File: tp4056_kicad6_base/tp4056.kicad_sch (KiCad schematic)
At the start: 23 parts, among them J1 USB_B_Micro, J2 Conn_01x01_Female, J3 Conn_01x01_Female, J4 Conn_01x01_Female, J5 Conn_01x01_Female, J6 Conn_01x01_Female, J7 Conn_01x01_Female, U1 TP4056, U2 DW01

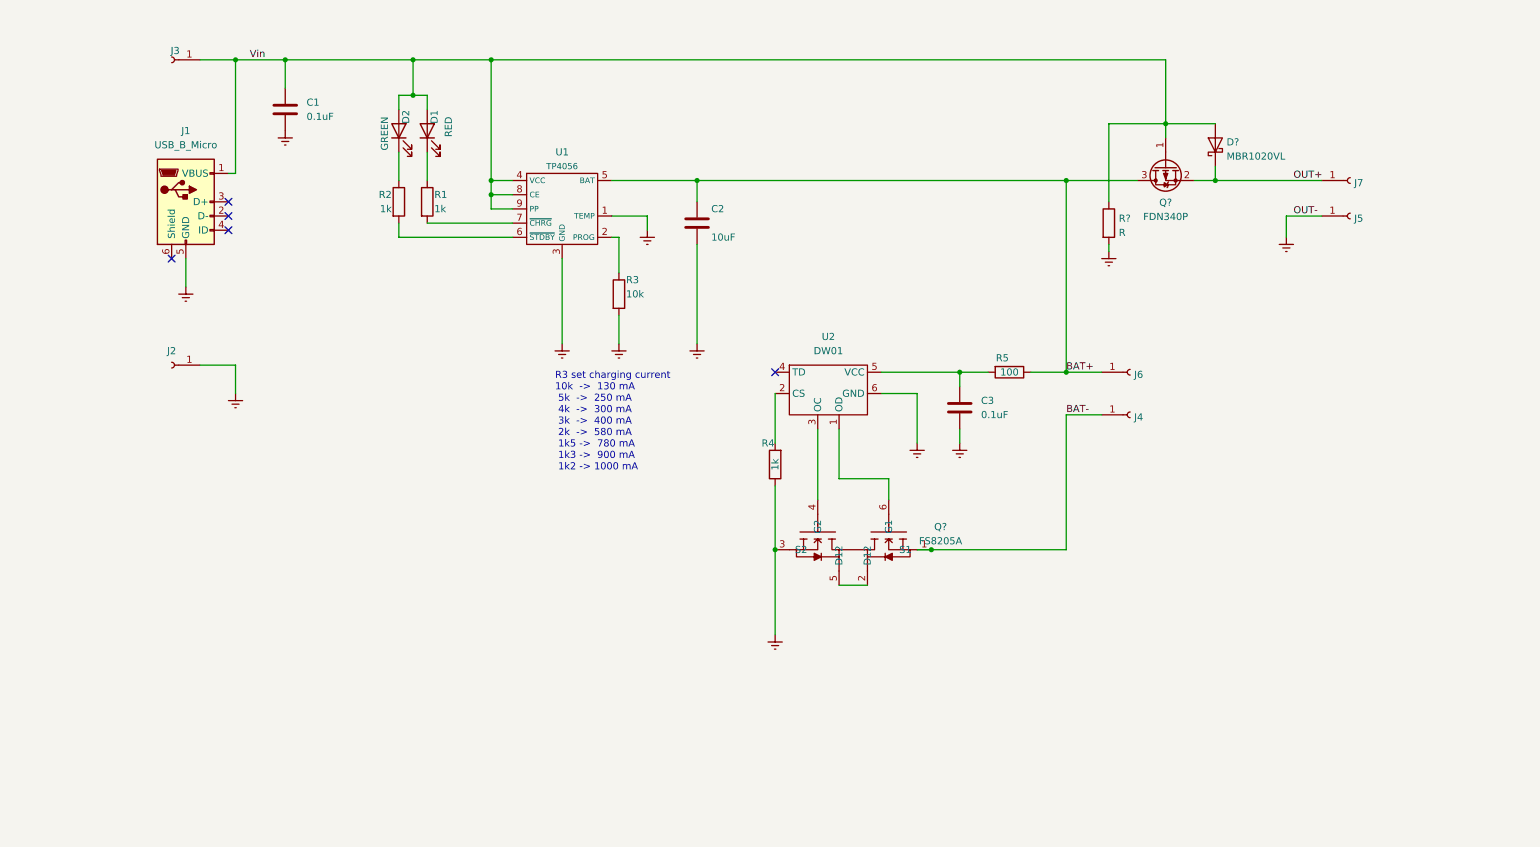
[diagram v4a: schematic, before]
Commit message: add 3v3 regulator
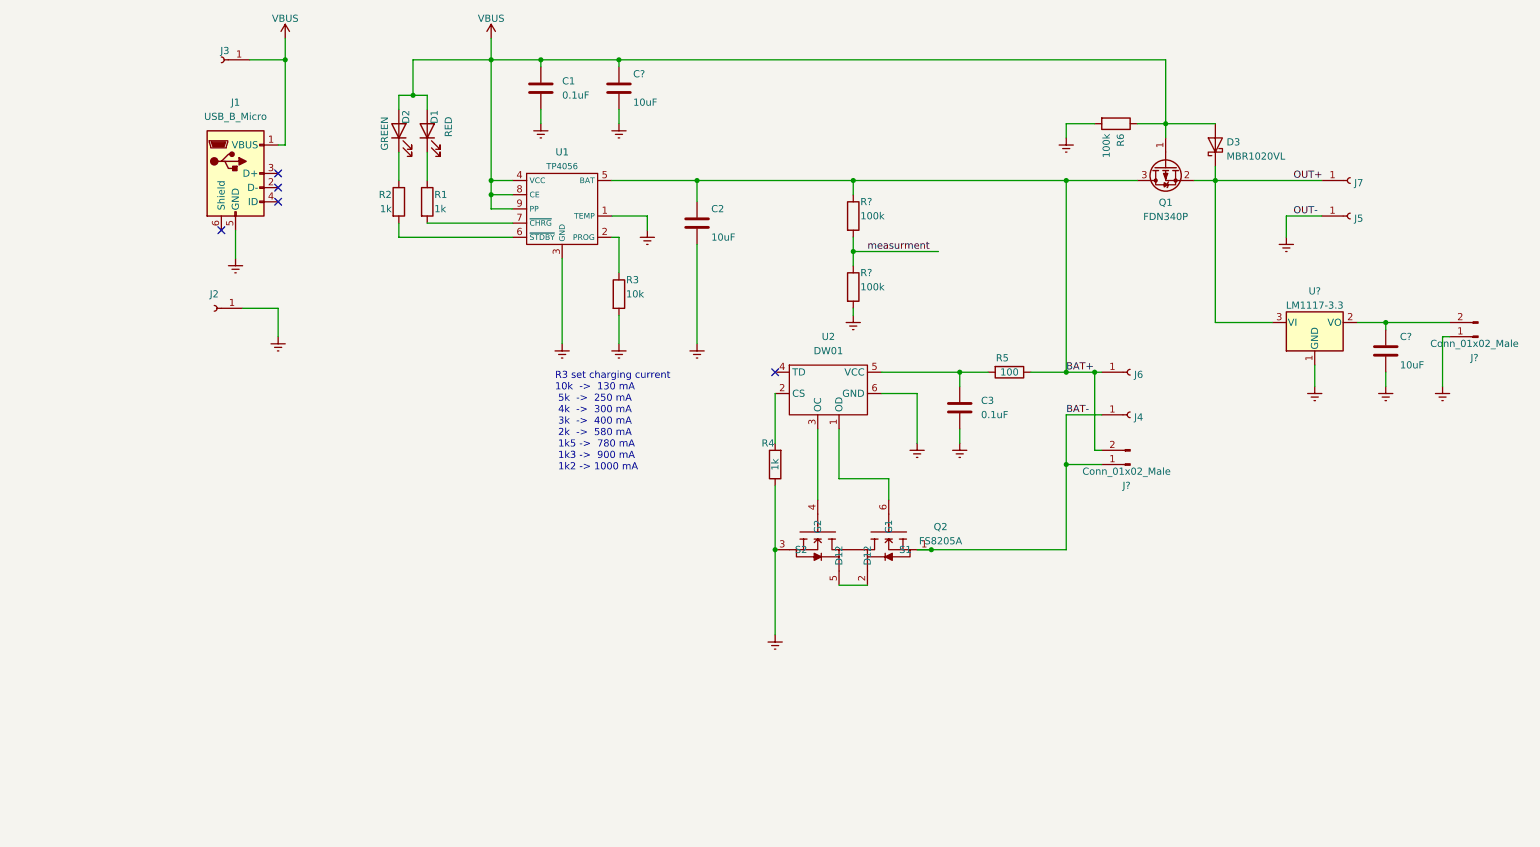
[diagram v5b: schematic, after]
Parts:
- added C? (x2): 10uF, Capacitor_SMD:C_0805_2012Metric_Pad1.18x1.45mm_HandSolder, symbol Device:C
- added J? (x2): Conn_01x02_Male, symbol Connector:Conn_01x02_Male
- added R? (x2): 100k, Resistor_SMD:R_0805_2012Metric_Pad1.20x1.40mm_HandSolder, symbol Device:R
- added U?: LM1117-3.3, symbol Regulator_Linear:LM1117-3.3
- R6: renamed from R?; value R -> 100k; footprint (none) -> Resistor_SMD:R_0805_2012Metric_Pad1.20x1.40mm_HandSolder
- gave numbers to parts that had none: 3
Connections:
- net BAT+: now also J?.2 (Pin_2), R?.1
- net BAT-: now also J?.1 (Pin_1)
- net Earth: now also C?.2, C?.2, J?.1 (Pin_1), R?.2, U?.1 (GND)
- net OUT+: now also U?.3 (VI)
- net Vin renamed VBUS
- net VBUS: now also C?.1
- new net: C?.1, J?.2 (Pin_2), U?.2 (VO)
- new net measurment: R?.1, R?.2
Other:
- moved on the sheet: C1, J1, J2, J3, R6

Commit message: Add 3.3V LDO regulator
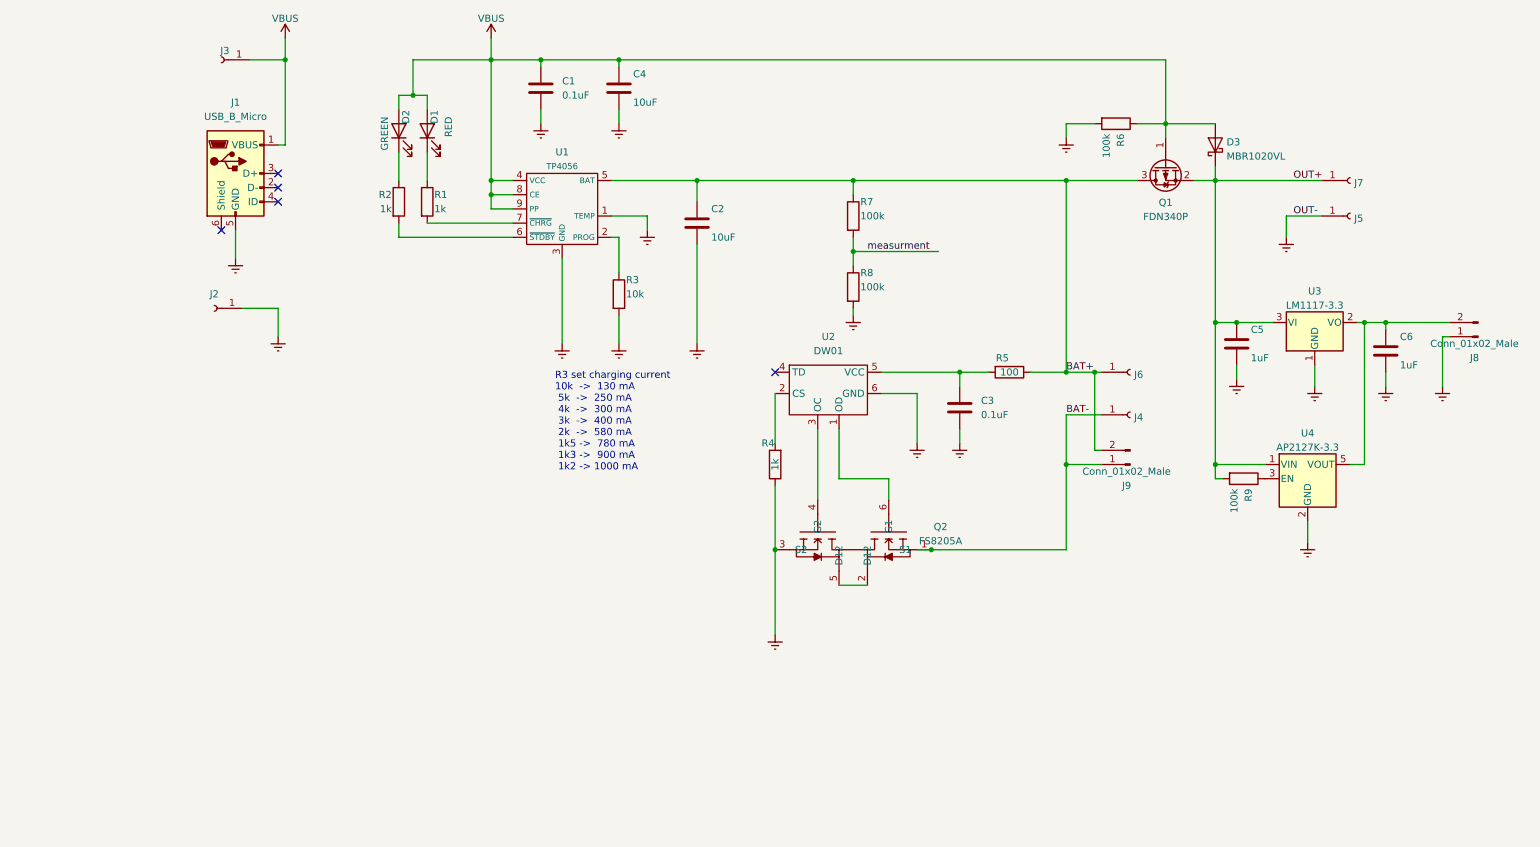
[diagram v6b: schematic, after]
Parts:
- added C5: 1uF, Capacitor_SMD:C_0805_2012Metric_Pad1.18x1.45mm_HandSolder, symbol Device:C
- added R9: 100k, Resistor_SMD:R_0805_2012Metric_Pad1.20x1.40mm_HandSolder, symbol Device:R
- added U4: AP2127K-3.3, Package_TO_SOT_SMD:SOT-23-5, symbol Regulator_Linear:AP2127K-3.3
- C6: renamed from C?; value 10uF -> 1uF
- gave numbers to parts that had none: 6
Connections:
- net Earth: now also C5.2, U4.2 (GND)
- net OUT+: now also C5.1, R9.2, U4.1 (VIN)
- net at C6.1, J8.2 (Pin_2), U3.2 (VO): now also U4.5 (VOUT)
- new net: R9.1, U4.3 (EN)

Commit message: Cambios estéticos en el sch
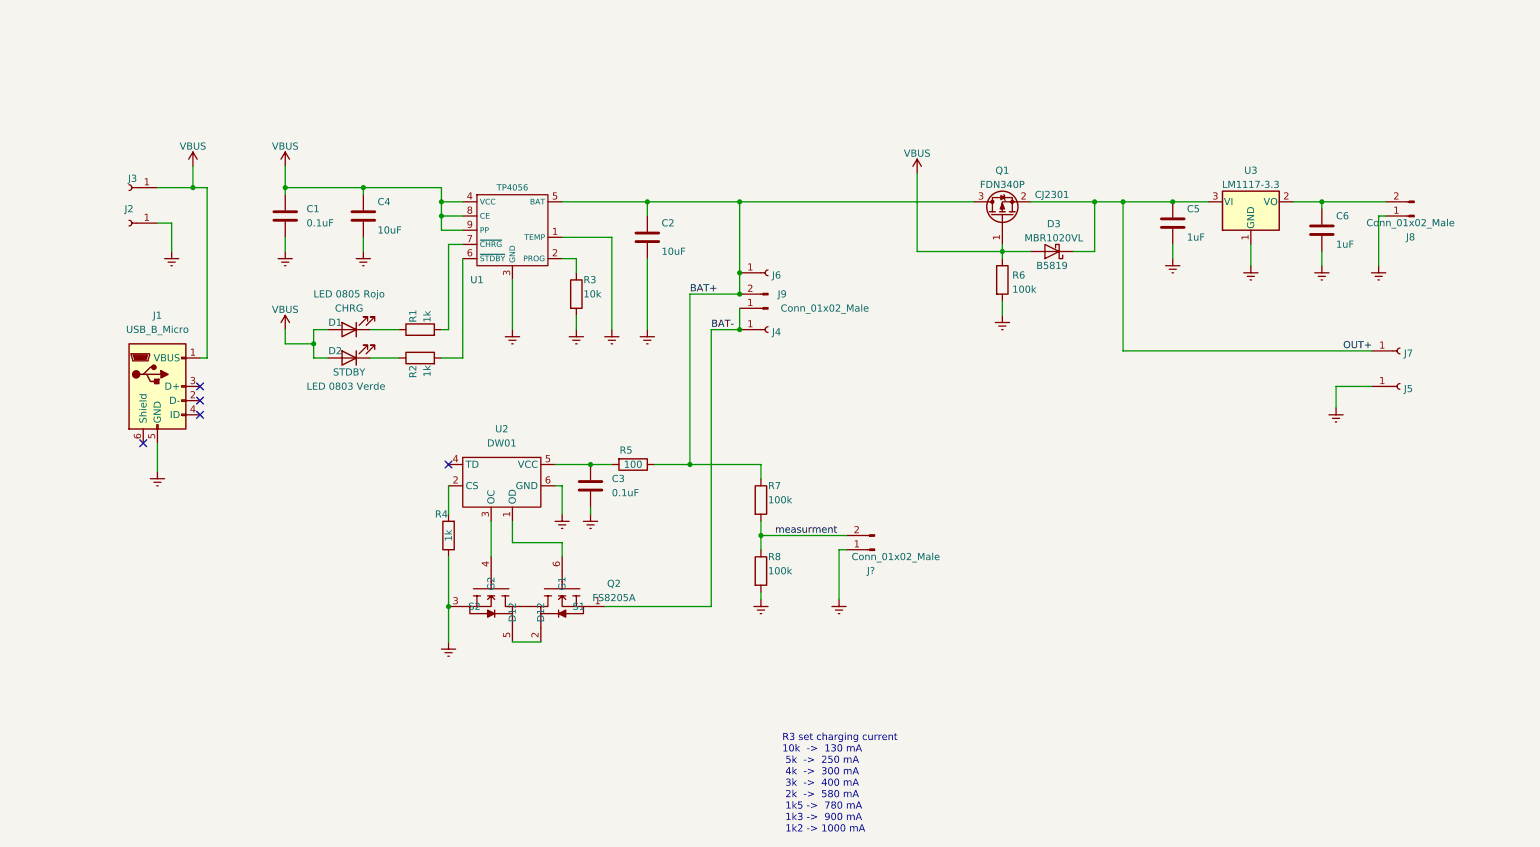
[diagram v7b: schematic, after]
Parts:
- removed R9: 100k, Resistor_SMD:R_0805_2012Metric_Pad1.20x1.40mm_HandSolder, symbol Device:R
- removed U4: AP2127K-3.3, Package_TO_SOT_SMD:SOT-23-5, symbol Regulator_Linear:AP2127K-3.3
- added J?: Conn_01x02_Male, Connector_PinHeader_2.54mm:PinHeader_1x02_P2.54mm_Vertical, symbol Connector:Conn_01x02_Male
- D1: value RED -> LED 0805 Rojo; Funcion (none) -> CHRG
- D2: value GREEN -> LED 0803 Verde; Función (none) -> STDBY
- D3: Alt (none) -> B5819
- J8: footprint (none) -> Connector_PinHeader_2.54mm:PinHeader_1x02_P2.54mm_Vertical
- J9: footprint (none) -> Connector_JST:JST_PH_B2B-PH-K_1x02_P2.00mm_Vertical
- Q1: Alt (none) -> CJ2301
- U3: footprint (none) -> Package_TO_SOT_SMD_AKL:SOT-23
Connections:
- net Earth: now also J?.1 (Pin_1)
- net measurment: now also J?.2 (Pin_2)
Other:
- moved on the sheet: C1, C2, C3, C4, C5, C6, D1, D2, D3, J1, J2, J3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

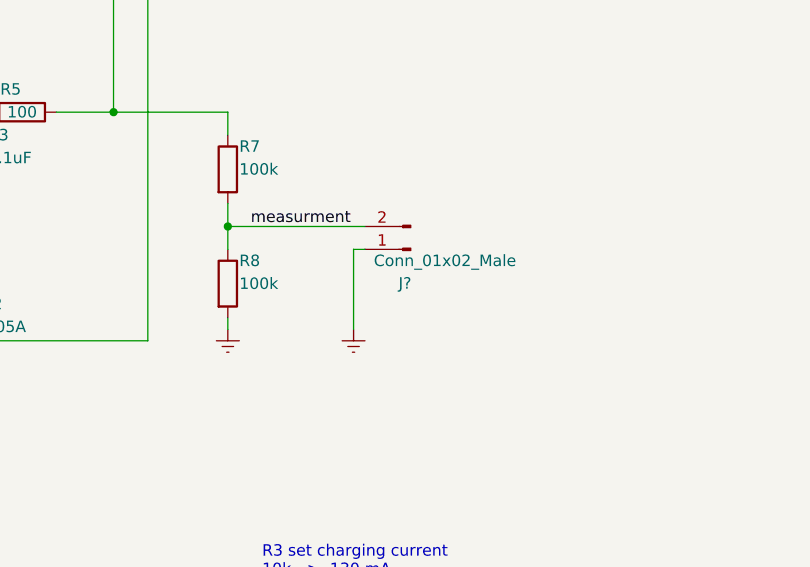
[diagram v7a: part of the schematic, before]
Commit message: pcd.Add board and position elements
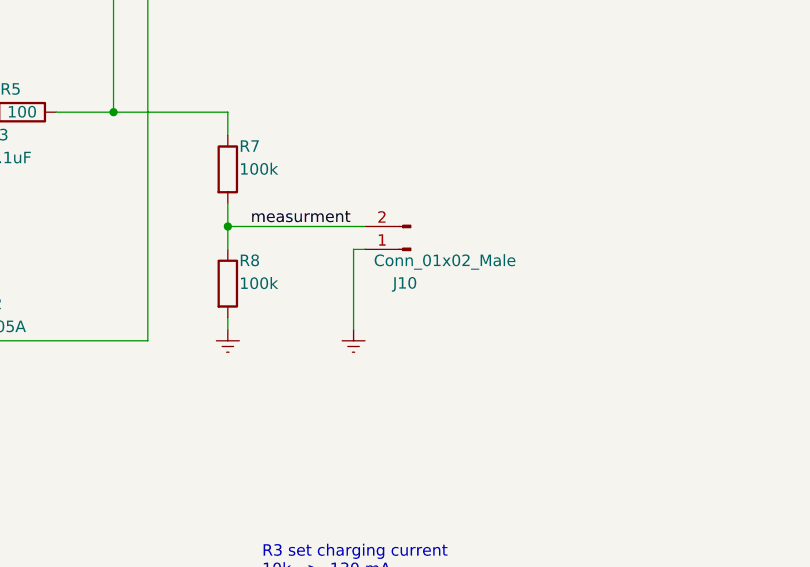
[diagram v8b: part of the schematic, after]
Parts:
- gave numbers to parts that had none: 1
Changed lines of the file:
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@@
   (symbol (lib_id "power:Earth") (at 161.29 151.13 0) (unit 1)
     (in_bom yes) (on_board yes) (fields_autoplaced)
-    (property "Reference" "#PWR?" (id 0) (at 161.29 157.48 0)
+    (property "Reference" "#PWR0122" (id 0) (at 161.29 157.48 0)
       (effects (font (size 1.27 1.27)) hide)
     )
@@
   (symbol (lib_id "power:VBUS") (at 175.26 74.93 0) (unit 1)
     (in_bom yes) (on_board yes) (fields_autoplaced)
-    (property "Reference" "#PWR?" (id 0) (at 175.26 78.74 0)
+    (property "Reference" "#PWR0121" (id 0) (at 175.26 78.74 0)
       (effects (font (size 1.27 1.27)) hide)
     )
@@
   (symbol (lib_id "Connector:Conn_01x02_Male") (at 167.64 142.24 180) (unit 1)
     (in_bom yes) (on_board yes)
-    (property "Reference" "J?" (id 0) (at 167.005 146.016 0))
+    (property "Reference" "J10" (id 0) (at 167.005 146.016 0))
     (property "Value" "Conn_01x02_Male" (id 1) (at 171.45 143.51 0))
     (property "Footprint" "Connector_PinHeader_2.54mm:PinHeader_1x02_P2.54mm_Vertical" (id 2) (at 167.64 142.24 0)
@@
   (symbol (lib_id "power:VBUS") (at 62.23 102.87 0) (unit 1)
     (in_bom yes) (on_board yes) (fields_autoplaced)
-    (property "Reference" "#PWR?" (id 0) (at 62.23 106.68 0)
+    (property "Reference" "#PWR0116" (id 0) (at 62.23 106.68 0)
       (effects (font (size 1.27 1.27)) hide)
     )
@@
       (reference "#PWR0115") (unit 1) (value "Earth") (footprint "")
     )
+    (path "/f30262f4-97a0-412f-adbd-a96dac14ce7c"
+      (reference "#PWR0116") (unit 1) (value "VBUS") (footprint "")
+    )
     (path "/cc76a413-0301-44c6-a985-e91d6961a6b5"
       (reference "#PWR0117") (unit 1) (value "Earth") (footprint "")
@@
       (reference "#PWR0120") (unit 1) (value "Earth") (footprint "")
     )
+    (path "/89732b9c-d18e-4ab2-8db9-768b9bb052e6"
+      (reference "#PWR0121") (unit 1) (value "VBUS") (footprint "")
+    )
     (path "/6cf81304-5a9a-4346-98cf-ebdc3d6cc2d1"
-      (reference "#PWR?") (unit 1) (value "Earth") (footprint "")
-    )
-    (path "/89732b9c-d18e-4ab2-8db9-768b9bb052e6"
-      (reference "#PWR?") (unit 1) (value "VBUS") (footprint "")
-    )
-    (path "/f30262f4-97a0-412f-adbd-a96dac14ce7c"
-      (reference "#PWR?") (unit 1) (value "VBUS") (footprint "")
+      (reference "#PWR0122") (unit 1) (value "Earth") (footprint "")
     )
     (path "/7870a9db-0a4b-4ce4-a426-dcf645359822"
@@
     )
     (path "/987e29f2-3f08-41f0-9703-e9389e408646"
-      (reference "J?") (unit 1) (value "Conn_01x02_Male") (footprint "Connector_PinHeader_2.54mm:PinHeader_1x02_P2.54mm_Vertical")
+      (reference "J10") (unit 1) (value "Conn_01x02_Male") (footprint "Connector_PinHeader_2.54mm:PinHeader_1x02_P2.54mm_Vertical")
     )
     (path "/be2f32b9-4a16-4a93-bf7d-d4847547881d"
